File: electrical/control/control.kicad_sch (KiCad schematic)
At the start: 42 parts, among them J1 USB4105-GF-A, J3 SWD, J4 QWIIC, J5 TC2030-NL, J6 UART, SW1 SYS, U1 RP2040, U2 ABPMRRV001PD2A3, U4 W25Q16JVSSIQ, U5 LP5907MFX-3.3, Y1 ABM8-272-T3

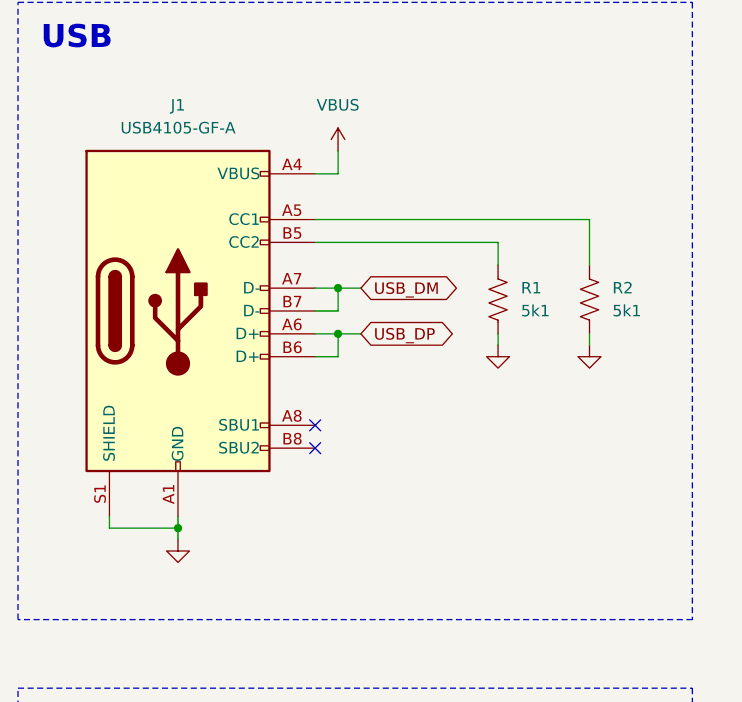
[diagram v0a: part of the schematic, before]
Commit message: Add power flags for VBUS and GND
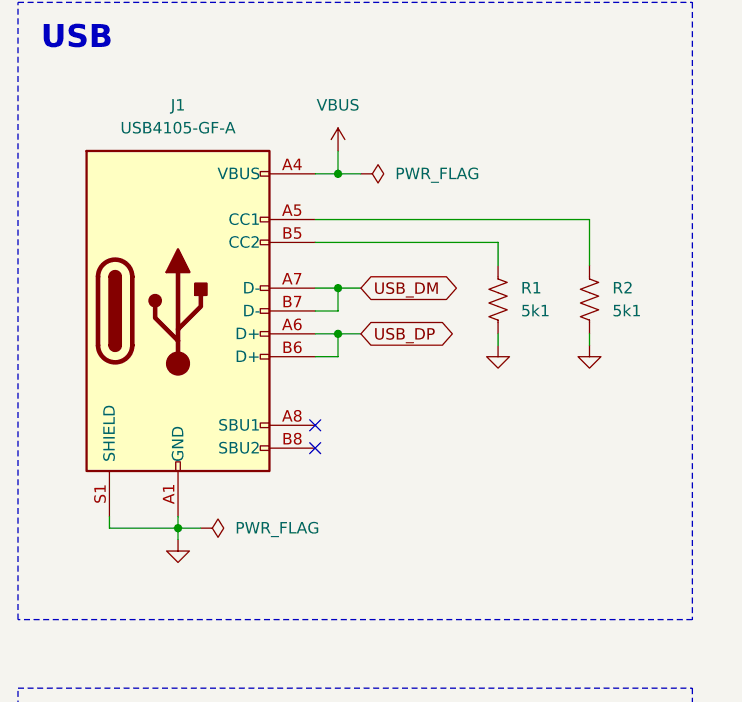
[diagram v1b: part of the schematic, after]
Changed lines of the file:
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@@
 	)
 	(junction
+		(at 77.47 69.85)
+		(diameter 0)
+		(color 0 0 0 0)
+	)
+	(junction
 		(at 274.32 69.85)
 		(diameter 0)
@@
 	(wire
 		(pts
+			(xy 80.01 69.85) (xy 77.47 69.85)
+		)
+		(stroke
+			(width 0)
+			(type default)
+		)
+	)
+	(wire
+		(pts
 			(xy 77.47 157.48) (xy 77.47 156.21)
 		)
@@
 	(wire
 		(pts
+			(xy 59.69 109.22) (xy 62.23 109.22)
+		)
+		(stroke
+			(width 0)
+			(type default)
+		)
+	)
+	(wire
+		(pts
 			(xy 154.94 69.85) (xy 170.18 69.85)
 		)
@@
 	)
 	(symbol
+		(lib_id "power:PWR_FLAG")
+		(at 62.23 109.22 270)
+		(unit 1)
+		(exclude_from_sim no)
+		(in_bom yes)
+		(on_board yes)
+		(dnp no)
+		(fields_autoplaced yes)
+		(property "Reference" "#FLG02"
+			(at 64.135 109.22 0)
+			(effects
+				(font
+					(size 1.27 1.27)
+				)
+				(hide yes)
+			)
+		)
+		(property "Value" "PWR_FLAG"
+			(at 66.04 109.2199 90)
+			(effects
+				(font
+					(size 1.27 1.27)
+				)
+				(justify left)
+			)
+		)
+		(property "Footprint" ""
+			(at 62.23 109.22 0)
+			(effects
+				(font
+					(size 1.27 1.27)
+				)
+				(hide yes)
+			)
+		)
+		(property "Datasheet" "~"
+			(at 62.23 109.22 0)
+			(effects
+				(font
+					(size 1.27 1.27)
+				)
+				(hide yes)
+			)
+		)
+		(property "Description" "Special symbol for telling ERC where power comes from"
+			(at 62.23 109.22 0)
+			(effects
+				(font
+					(size 1.27 1.27)
+				)
+				(hide yes)
+			)
+		)
+		(pin "1"
+		)
+		(instances
+			(project "control"
+				(path "/da26d94e-7a50-4b99-9678-5aaaf6987a15"
+					(reference "#FLG02")
+					(unit 1)
+				)
+			)
+		)
+	)
+	(symbol
 		(lib_id "Device:C")
 		(at 215.9 76.2 0)
@@
 					(unit 1)
 				)
+			)
+		)
+	)
+	(symbol
+		(lib_id "power:PWR_FLAG")
+		(at 80.01 69.85 270)
+		(unit 1)
+		(exclude_from_sim no)
+		(in_bom yes)
+		(on_board yes)
+		(dnp no)
+		(fields_autoplaced yes)
+		(property "Reference" "#FLG01"
+			(at 81.915 69.85 0)
+			(effects
+				(font
+					(size 1.27 1.27)
+				)
+				(hide yes)
+			)
+		)
+		(property "Value" "PWR_FLAG"
+			(at 83.82 69.8499 90)
+			(effects
+				(font
+					(size 1.27 1.27)
+				)
+				(justify left)
+			)
+		)
+		(property "Footprint" ""
+			(at 80.01 69.85 0)
+			(effects
+				(font
+					(size 1.27 1.27)
+				)
+				(hide yes)
+			)
+		)
+		(property "Datasheet" "~"
+			(at 80.01 69.85 0)
+			(effects
+				(font
+					(size 1.27 1.27)
+				)
+				(hide yes)
+			)
+		)
+		(property "Description" "Special symbol for telling ERC where power comes from"
+			(at 80.01 69.85 0)
+			(effects
+				(font
+					(size 1.27 1.27)
+				)
+				(hide yes)
+			)
+		)
+		(pin "1"
+		)
+		(instances
+			(project ""
+				(path "/da26d94e-7a50-4b99-9678-5aaaf6987a15"
+					(reference "#FLG01")
+					(unit 1)
+				)

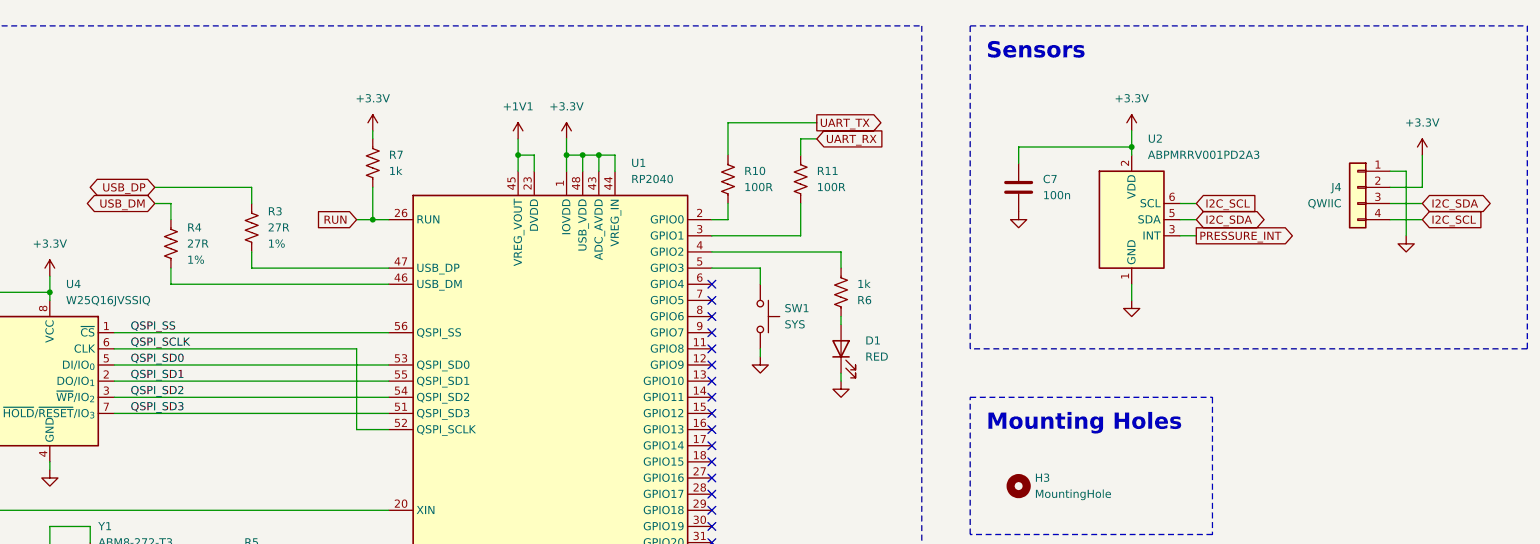
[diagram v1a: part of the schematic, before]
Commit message: Add custom symbol library; change 1uF caps
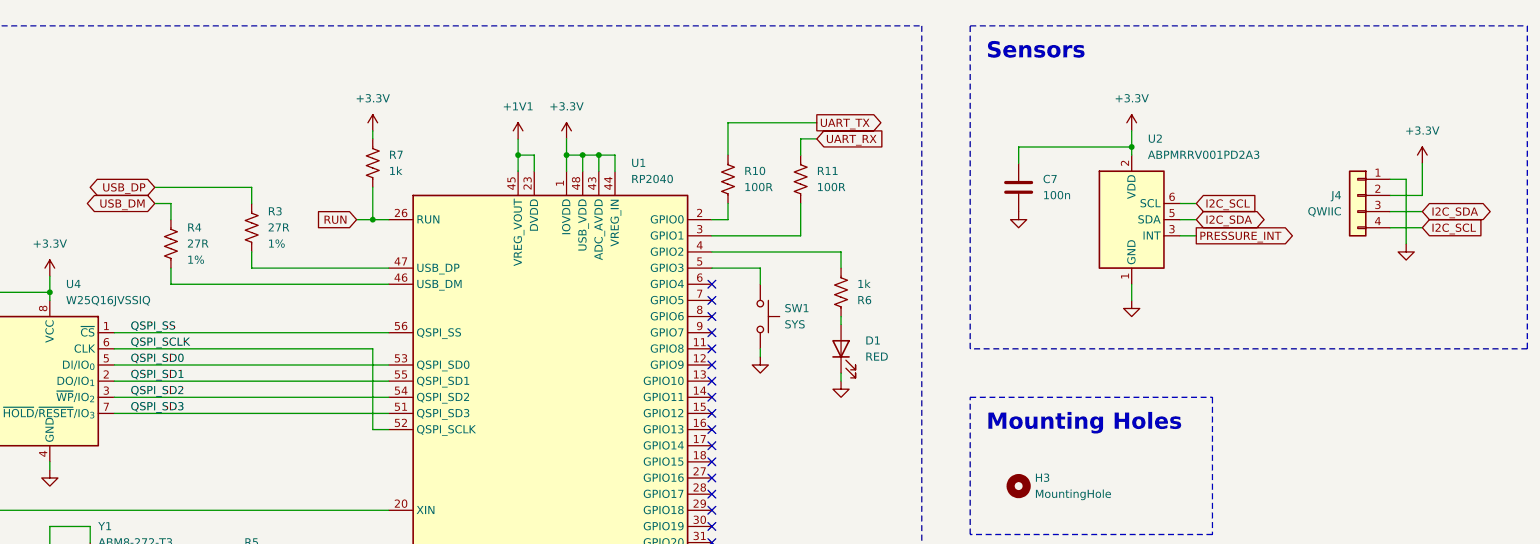
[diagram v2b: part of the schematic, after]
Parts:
- C4, C5, C8, C9: footprint Capacitor_SMD:C_0402_1005Metric -> Capacitor_SMD:C_0603_1608Metric; LCSC C52923 -> C29936
- U2: symbol Sensor_Pressure:XGZP6899D -> midi_concertina:ABPMRRV001PD2A3
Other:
- moved on the sheet: J4
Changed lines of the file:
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@@
 	(wire
 		(pts
-			(xy 372.11 128.27) (xy 367.03 128.27)
+			(xy 372.11 129.54) (xy 367.03 129.54)
 		)
 		(stroke
@@
 	(wire
 		(pts
-			(xy 367.03 130.81) (xy 372.11 130.81)
+			(xy 367.03 132.08) (xy 372.11 132.08)
 		)
 		(stroke
@@
 	(wire
 		(pts
-			(xy 166.37 151.13) (xy 204.47 151.13)
+			(xy 166.37 151.13) (xy 207.01 151.13)
 		)
 		(stroke
@@
 	(wire
 		(pts
-			(xy 204.47 151.13) (xy 204.47 163.83)
+			(xy 207.01 151.13) (xy 207.01 163.83)
 		)
 		(stroke
@@
 	(wire
 		(pts
-			(xy 372.11 125.73) (xy 372.11 120.65)
+			(xy 372.11 127) (xy 372.11 121.92)
 		)
 		(stroke
@@
 	(wire
 		(pts
-			(xy 367.03 125.73) (xy 372.11 125.73)
+			(xy 367.03 127) (xy 372.11 127)
 		)
 		(stroke
@@
 	(wire
 		(pts
-			(xy 204.47 163.83) (xy 209.55 163.83)
+			(xy 207.01 163.83) (xy 209.55 163.83)
 		)
 		(stroke
@@
 	(wire
 		(pts
-			(xy 369.57 123.19) (xy 369.57 133.35)
+			(xy 369.57 124.46) (xy 369.57 134.62)
 		)
 		(stroke
@@
 	(wire
 		(pts
-			(xy 367.03 123.19) (xy 369.57 123.19)
+			(xy 367.03 124.46) (xy 369.57 124.46)
 		)
 		(stroke
@@
 	(global_label "I2C_SCL"
 		(shape input)
-		(at 372.11 130.81 0)
+		(at 372.11 132.08 0)
 		(fields_autoplaced yes)
 		(effects
@@
 		)
 		(property "Intersheetrefs" "${INTERSHEET_REFS}"
-			(at 382.6547 130.81 0)
+			(at 382.6547 132.08 0)
 			(effects
 				(font
@@
 	(global_label "I2C_SDA"
 		(shape bidirectional)
-		(at 372.11 128.27 0)
+		(at 372.11 129.54 0)
 		(fields_autoplaced yes)
 		(effects
@@
 		)
 		(property "Intersheetrefs" "${INTERSHEET_REFS}"
-			(at 383.8265 128.27 0)
+			(at 383.8265 129.54 0)
 			(effects
 				(font
@@
 	(symbol
 		(lib_id "power:+3.3V")
-		(at 372.11 120.65 0)
+		(at 372.11 121.92 0)
 		(mirror y)
 		(unit 1)
@@
 		(fields_autoplaced yes)
 		(property "Reference" "#PWR019"
-			(at 372.11 124.46 0)
+			(at 372.11 125.73 0)
 			(effects
 				(font
@@
 		)
 		(property "Value" "+3.3V"
-			(at 372.11 115.57 0)
+			(at 372.11 116.84 0)
 			(effects
 				(font
@@
 		)
 		(property "Footprint" ""
-			(at 372.11 120.65 0)
+			(at 372.11 121.92 0)
 			(effects
 				(font
@@
 		)
 		(property "Datasheet" ""
-			(at 372.11 120.65 0)
+			(at 372.11 121.92 0)
 			(effects
 				(font
@@
 		)
 		(property "Description" "Power symbol creates a global label with name \"+3.3V\""
-			(at 372.11 120.65 0)
+			(at 372.11 121.92 0)
 			(effects
 				(font
@@
 	(symbol
 		(lib_id "Connector_Generic:Conn_01x04")
-		(at 361.95 125.73 0)
+		(at 361.95 127 0)
 		(mirror y)
 		(unit 1)
@@
 		(dnp no)
 		(property "Reference" "J4"
-			(at 359.41 125.73 0)
+			(at 359.41 127 0)
 			(effects
 				(font
@@
 		)
 		(property "Value" "QWIIC"
-			(at 359.41 128.27 0)
+			(at 359.41 129.54 0)
 			(effects
 				(font
@@
 		)
 		(property "Footprint" "Connector_JST:JST_SH_SM04B-SRSS-TB_1x04-1MP_P1.00mm_Horizontal"
-			(at 361.95 125.73 0)
+			(at 361.95 127 0)
 			(effects
 				(font
@@
 		)
 		(property "Datasheet" "~"
-			(at 361.95 125.73 0)
+			(at 361.95 127 0)
 			(effects
 				(font
@@
 		)
 		(property "Description" "Generic connector, single row, 01x04, script generated (kicad-library-utils/schlib/autogen/connector/)"
-			(at 361.95 125.73 0)
+			(at 361.95 127 0)
 			(effects
 				(font
@@
 		)
 		(property "LCSC" "C160404"
-			(at 361.95 125.73 0)
+			(at 361.95 127 0)
 			(effects
 				(font
@@
 			)
 		)
-		(property "Footprint" "Capacitor_SMD:C_0402_1005Metric"
+		(property "Footprint" "Capacitor_SMD:C_0603_1608Metric"
 			(at 354.0252 80.01 0)
 			(effects
@@
 			)
 		)
-		(property "LCSC" "C52923"
+		(property "LCSC" "C29936"
 			(at 353.06 76.2 0)
 			(effects
@@
 			)
 		)
-		(property "Footprint" "Capacitor_SMD:C_0402_1005Metric"
+		(property "Footprint" "Capacitor_SMD:C_0603_1608Metric"
 			(at 60.6552 156.21 0)
 			(effects
@@
 			)
 		)
-		(property "LCSC" "C52923"
+		(property "LCSC" "C29936"
 			(at 59.69 152.4 0)
 			(effects
@@
 	)
 	(symbol
-		(lib_id "Sensor_Pressure:XGZP6899D")
+		(lib_id "midi_concertina:ABPMRRV001PD2A3")
 		(at 326.39 130.81 0)
 		(unit 1)
@@
 			)
 		)
-		(property "Footprint" "Capacitor_SMD:C_0402_1005Metric"
+		(property "Footprint" "Capacitor_SMD:C_0603_1608Metric"
 			(at 310.8452 80.01 0)
 			(effects
@@
 			)
 		)
-		(property "LCSC" "C52923"
+		(property "LCSC" "C29936"
 			(at 309.88 76.2 0)
 			(effects
@@
 	(symbol
 		(lib_id "power:GND")
-		(at 369.57 133.35 0)
+		(at 369.57 134.62 0)
 		(mirror y)
 		(unit 1)
@@
 		(fields_autoplaced yes)
 		(property "Reference" "#PWR018"
-			(at 369.57 139.7 0)
+			(at 369.57 140.97 0)
 			(effects
 				(font
@@
 		)
 		(property "Value" "GND"
-			(at 369.57 138.43 0)
+			(at 369.57 139.7 0)
 			(effects
 				(font
@@
 		)
 		(property "Footprint" ""
-			(at 369.57 133.35 0)
+			(at 369.57 134.62 0)
 			(effects
 				(font
@@
 		)
 		(property "Datasheet" ""
-			(at 369.57 133.35 0)
+			(at 369.57 134.62 0)
 			(effects
 				(font
@@
 		)
 		(property "Description" "Power symbol creates a global label with name \"GND\" , ground"
-			(at 369.57 133.35 0)
+			(at 369.57 134.62 0)
 			(effects
 				(font
@@
 			)
 		)
-		(property "Footprint" "Capacitor_SMD:C_0402_1005Metric"
+		(property "Footprint" "Capacitor_SMD:C_0603_1608Metric"
 			(at 96.2152 156.21 0)
 			(effects
@@
 			)
 		)
-		(property "LCSC" "C52923"
+		(property "LCSC" "C29936"
 			(at 95.25 152.4 0)
 			(effects

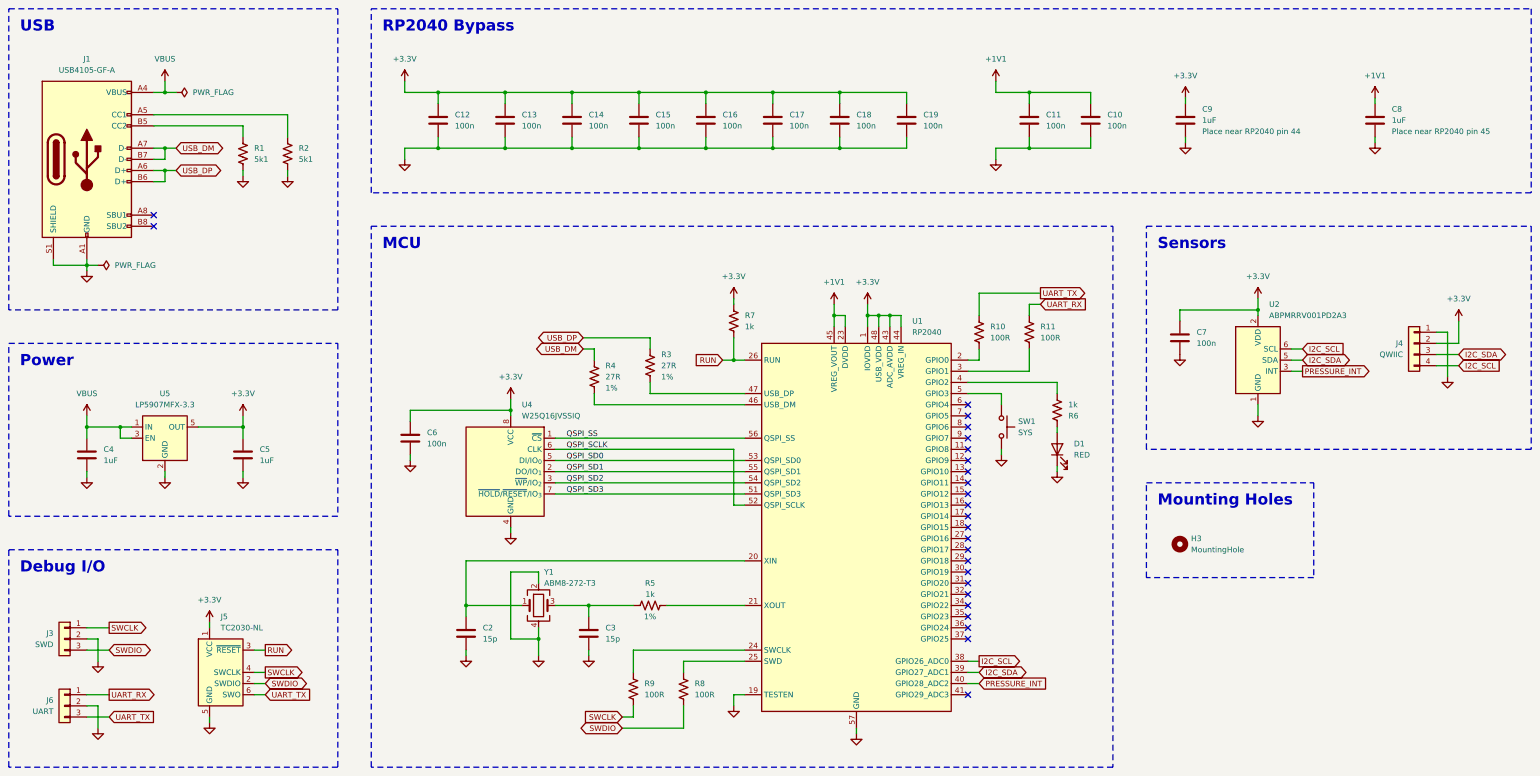
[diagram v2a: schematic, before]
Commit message: Reassign annotations
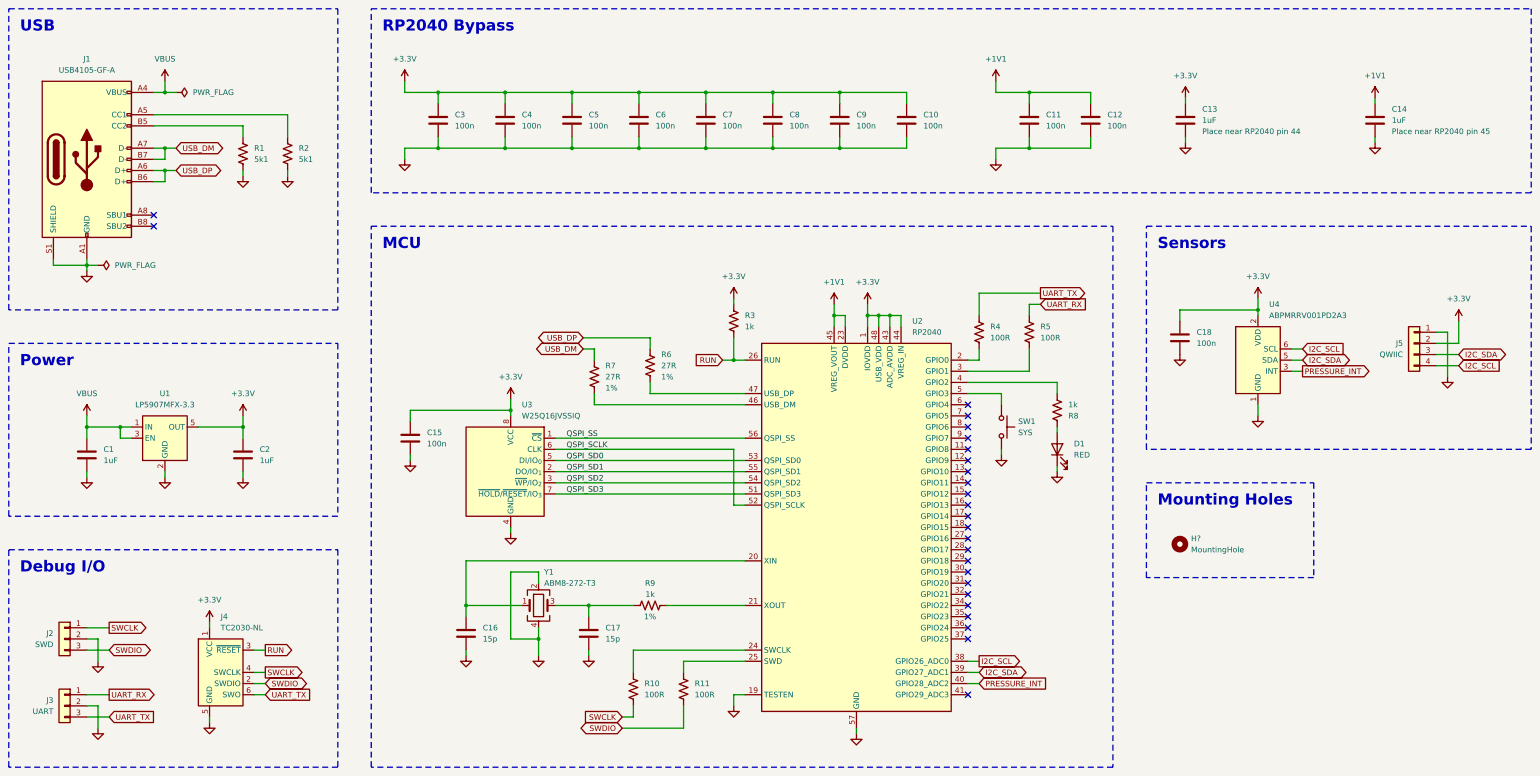
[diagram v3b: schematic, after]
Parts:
- renumbered C4 to C1, C19 to C10, C10 to C12, C9 to C13, C8 to C14, C6 to C15, C2 to C16, C3 to C17, C7 to C18, C5 to C2, C12 to C3, C13 to C4, C14 to C5, C15 to C6, C16 to C7, C17 to C8, C18 to C9, H3 to H?, J3 to J2, J6 to J3, J5 to J4, J4 to J5, R9 to R10, R8 to R11, R7 to R3, R10 to R4, R11 to R5, R3 to R6, R4 to R7, R6 to R8, R5 to R9, U5 to U1, U1 to U2, U4 to U3, U2 to U4

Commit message: Add footprint lib; various other changes
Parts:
- removed U4: ABPMRRV001PD2A3, Sensor_Pressure:CFSensor_XGZP6899x, symbol midi_concertina:ABPMRRV001PD2A3
- added U4: ABPMRRV060MG2A3, midi_concertina:Honeywell_ABPMRRx, symbol midi_concertina:ABPMRRV060MG2A3
- gave numbers to parts that had none: 1
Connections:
- net +3.3V: now also U4.2 (VDD)
- net GND: now also U4.1 (GND)
- net I2C_SCL: now also U4.6 (SCL)
- net I2C_SDA: now also U4.5 (SDA)
- net PRESSURE_INT: now also U4.3 (INT)

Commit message: USB PCB layout
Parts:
- removed C10: 100n, Capacitor_SMD:C_0402_1005Metric, symbol Device:C
- removed J2: SWD, Connector_JST:JST_SH_SM03B-SRSS-TB_1x03-1MP_P1.00mm_Horizontal, symbol Connector_Generic:Conn_01x03
- removed J3: UART, Connector_JST:JST_SH_SM03B-SRSS-TB_1x03-1MP_P1.00mm_Horizontal, symbol Connector_Generic:Conn_01x03
- removed J5: QWIIC, Connector_JST:JST_SH_SM04B-SRSS-TB_1x04-1MP_P1.00mm_Horizontal, symbol Connector_Generic:Conn_01x04
- removed U1: LP5907MFX-3.3, Package_TO_SOT_SMD:SOT-23-5, symbol Regulator_Linear:LP5907MFX-3.3
- added C3: 1uF, Capacitor_SMD:C_0402_1005Metric, symbol Device:C
- added J2: SWD, Connector_JST:JST_SH_SM03B-SRSS-TB_1x03-1MP_P1.00mm_Horizontal, symbol Connector_Generic_MountingPin:Conn_01x03_MountingPin
- added J4: UART, Connector_JST:JST_SH_SM03B-SRSS-TB_1x03-1MP_P1.00mm_Horizontal, symbol Connector_Generic_MountingPin:Conn_01x03_MountingPin
- added J5: QWIIC, Connector_JST:JST_SH_SM04B-SRSS-TB_1x04-1MP_P1.00mm_Horizontal, symbol Connector_Generic_MountingPin:Conn_01x04_MountingPin
- added U1: USBLC6-2P6, Package_TO_SOT_SMD:SOT-666, symbol Power_Protection:USBLC6-2P6
- added U2: LP5912-3.3DRV, Package_SON:WSON-6-1EP_2x2mm_P0.65mm_EP1x1.6mm_ThermalVias, symbol Regulator_Linear:LP5912-3.3DRV
- C1: value 1uF -> 100n; footprint Capacitor_SMD:C_0603_1608Metric -> Capacitor_SMD:C_0402_1005Metric; LCSC C29936 -> C1525
- C13, C14, C2: footprint Capacitor_SMD:C_0603_1608Metric -> Capacitor_SMD:C_0402_1005Metric; LCSC C29936 -> C528974
- renumbered C9 to C10, C3 to C4, C4 to C5, C5 to C6, C6 to C7, C7 to C8, C8 to C9, J4 to J3, R2 to R1, R1 to R2, U2 to U4, U4 to U5
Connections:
- net +3.3V: now also C3.1, J5.2 (Pin_2), U2.1 (OUT); no longer C2.1
- net GND: now also C3.2, J2.2 (Pin_2), J4.2 (Pin_2), J5.1 (Pin_1), U1.2 (GND), U2.3 (PG), U2.5 (GND), U2.7 (EP)
- net I2C_SCL: now also J5.4 (Pin_4)
- net I2C_SDA: now also J5.3 (Pin_3)
- net SWCLK: now also J2.1 (Pin_1)
- net SWDIO: now also J2.3 (Pin_3)
- net UART_RX: now also J4.1 (Pin_1)
- net UART_TX: now also J4.3 (Pin_3)
- net VBUS: now also C2.1, U1.5 (VBUS), U2.4 (EN), U2.6 (IN)
- net USB_DM: no longer names the net of J1.A7 (D-), J1.B7 (D-)
- net USB_DM: now also U1.1 (I/O1); no longer R7.2
- net USB_DP: no longer names the net of J1.A6 (D+), J1.B6 (D+)
- net USB_DP: now also U1.3 (I/O2); no longer R6.2
- new net USB_D+: R6.2, U1.4 (I/O2)
- new net USB_D-: R7.2, U1.6 (I/O1)
- no-connect marks 25 -> 28
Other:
- moved on the sheet: C11, C12, C13, J3, R1, R2

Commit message: More PCB layout
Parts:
- U3: value W25Q16JVSSIQ -> W25Q16JVSNIQ; footprint Package_SO:SOIC-8_5.3x5.3mm_P1.27mm -> Package_SO:SOIC-8_3.9x4.9mm_P1.27mm; LCSC C131025 -> C115407
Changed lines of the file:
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@@
 			)
 		)
-		(property "Value" "W25Q16JVSSIQ"
+		(property "Value" "W25Q16JVSNIQ"
 			(at 158.75 143.51 0)
 			(effects
@@
 			)
 		)
-		(property "Footprint" "Package_SO:SOIC-8_5.3x5.3mm_P1.27mm"
+		(property "Footprint" "Package_SO:SOIC-8_3.9x4.9mm_P1.27mm"
 			(at 156.21 156.21 0)
 			(effects
@@
 			)
 		)
-		(property "LCSC" "C131025"
+		(property "LCSC" "C115407"
 			(at 156.21 156.21 0)
 			(effects
